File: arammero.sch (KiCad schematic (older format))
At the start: 21 parts

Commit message: Improvements
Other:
- note added: "TODO pillanatérték?"
- note removed: "Kell másik műveleti erősítő: pl \nMC33204DR2G\nrail-to-rail, +-3.3V-ról fog járni, nagy közös módusú elnyomás"

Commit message: correct  op amp type to rail-to-rail
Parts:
- U6: renamed from U?; value TL084 -> mc33204
- gave numbers to parts that had none: 16

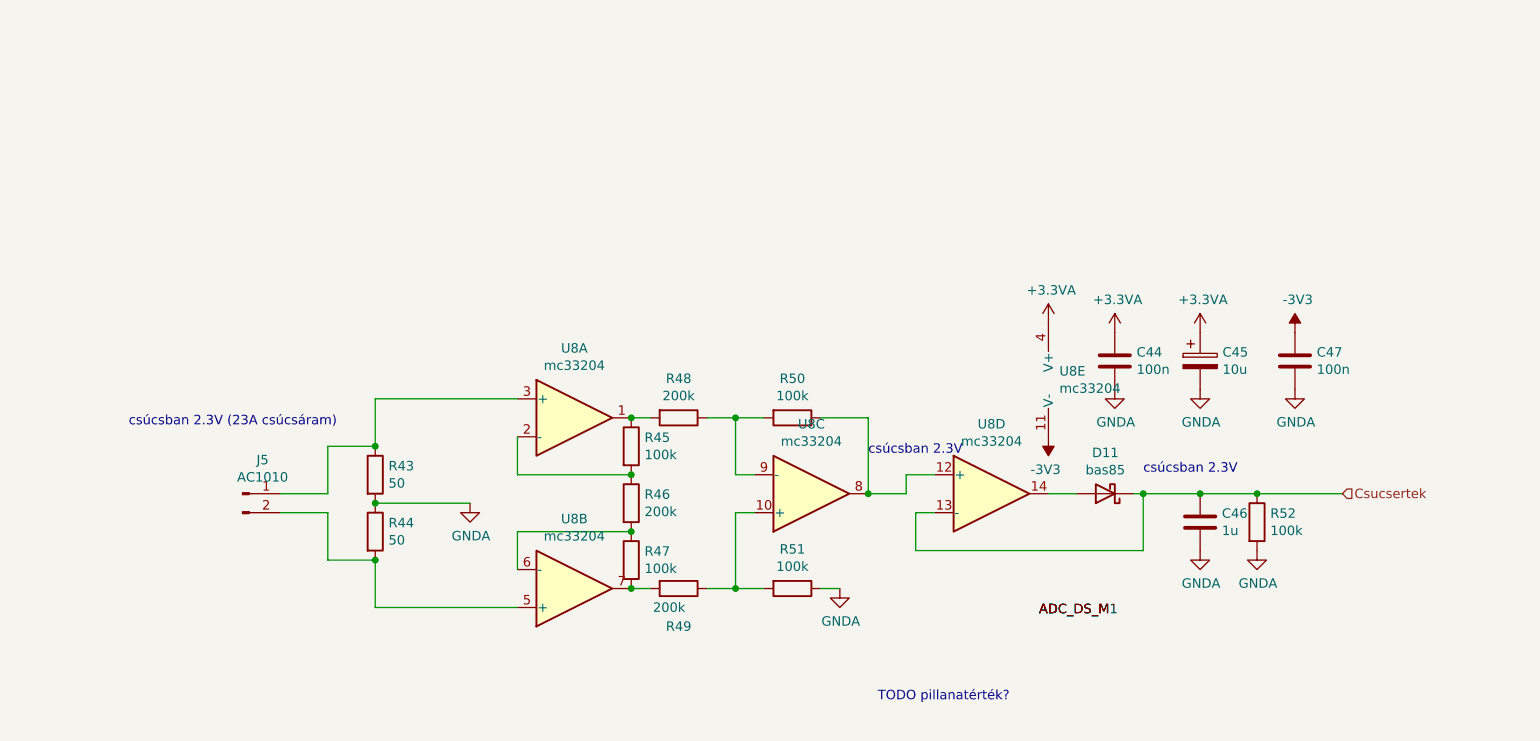
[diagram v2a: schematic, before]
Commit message: Tápegység külön lap + fázisméréshez áramkörök
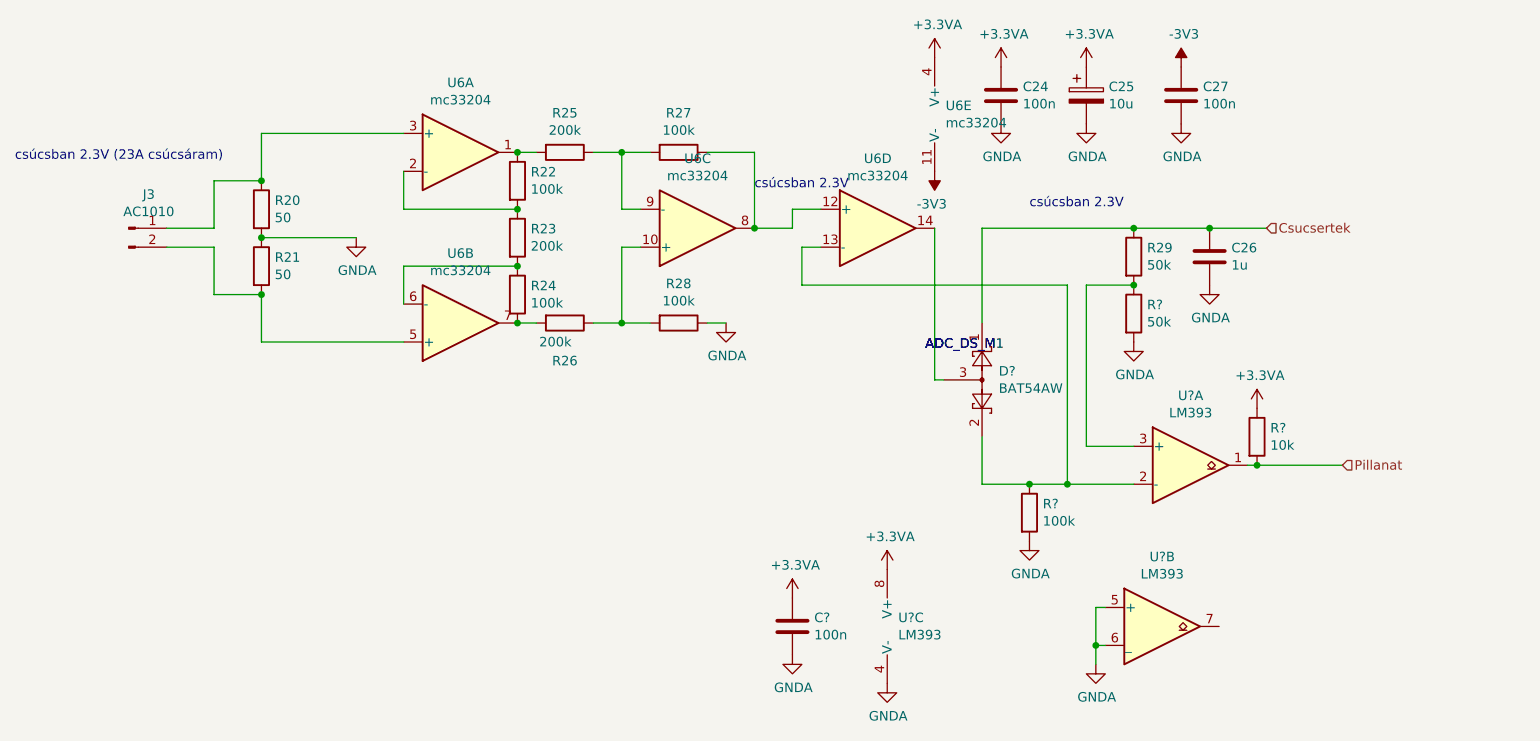
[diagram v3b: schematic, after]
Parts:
- removed D10: bas85, symbol Device:D_Schottky
- added C?: 100n, symbol Device:C
- added D?: BAT54AW, Package_TO_SOT_SMD:SOT-323_SC-70, symbol Diode:BAT54AW
- added R?: 50k, symbol Device:R
- added R?: 100k, symbol Device:R
- added R?: 10k, symbol Device:R
- added U? (x3): LM393, symbol Comparator:LM393
- R29: value 100k -> 50k
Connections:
- net +3.3VA: now also C?.1, R?.1, U?.8 (V+)
- net Csucsertek: now also D?.1; no longer U6.13 (-)
- net GNDA: now also C?.2, R?.2, R?.2, U?.4 (V-), U?.5 (+), U?.6 (_); no longer R29.2
- net at U6.14: now also D?.3
- new net: D?.2, R?.1, U6.13 (-), U?.2 (-)
- new net: R29.2, R?.1, U?.3 (+)
- new net Pillanat: R?.2, U?.1
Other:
- note removed: "TODO pillanatérték?"
- moved on the sheet: C24, C25, C26, C27, J3, R20, R21, R22, R23, R24, R25, R26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

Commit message: Testpoints + ground connections
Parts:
- added TP? (x4): TestPoint, symbol Connector:TestPoint
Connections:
- net Csucsertek: now also TP?.1
- net Pillanat: now also TP?.1
- net at R27.1, U6.12 (+), U6.8: now also TP?.1
- net at D?.2, R?.1, U6.13 (-)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: now also TP?.1
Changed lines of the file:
@@
 Csucsertek
 Wire Wire Line
-	5650 2600 5850 2600
+	5650 2600 5800 2600
 Text HLabel 8750 3850 2    50   Input ~ 0
 Pillanat
@@
 $EndComp
 Wire Wire Line
-	7650 2600 8050 2600
+	7650 2600 7900 2600
 Connection ~ 8050 2600
 Wire Wire Line
@@
 Connection ~ 8300 3850
 Wire Wire Line
-	8300 3850 8750 3850
+	8300 3850 8600 3850
 Wire Wire Line
 	7300 2900 7300 3950
@@
 	6850 3700 6850 3950
 Wire Wire Line
-	6850 3950 7100 3950
+	6850 3950 6900 3950
 Wire Wire Line
 	6850 3100 6850 2600
@@
 Wire Wire Line
 	6600 2600 6600 3400
+$Comp
+L Connector:TestPoint TP?
+U 1 1 5F898268
+P 5800 2650
+F 0 "TP?" H 5743 2676 50  0000 R CNN
+F 1 "TestPoint" H 5743 2767 50  0000 R CNN
+F 2 "" H 6000 2650 50  0001 C CNN
+F 3 "~" H 6000 2650 50  0001 C CNN
+	1    5800 2650
+	1    0    0    1
+$EndComp
+Wire Wire Line
+	5800 2650 5800 2600
+Connection ~ 5800 2600
+Wire Wire Line
+	5800 2600 5850 2600
+$Comp
+L Connector:TestPoint TP?
+U 1 1 5F89C1AC
+P 7900 2550
+F 0 "TP?" H 7842 2668 50  0000 R CNN
+F 1 "TestPoint" H 7842 2577 50  0000 R CNN
+F 2 "" H 8100 2550 50  0001 C CNN
+F 3 "~" H 8100 2550 50  0001 C CNN
+	1    7900 2550
+	-1   0    0    -1
+$EndComp
+Wire Wire Line
+	7900 2550 7900 2600
+Connection ~ 7900 2600
+Wire Wire Line
+	7900 2600 8050 2600
+$Comp
+L Connector:TestPoint TP?
+U 1 1 5F8A1D27
+P 8600 3800
+F 0 "TP?" H 8542 3918 50  0000 R CNN
+F 1 "TestPoint" H 8542 3827 50  0000 R CNN
+F 2 "" H 8800 3800 50  0001 C CNN
+F 3 "~" H 8800 3800 50  0001 C CNN
+	1    8600 3800
+	-1   0    0    -1
+$EndComp
+Wire Wire Line
+	8600 3800 8600 3850
+Connection ~ 8600 3850
+Wire Wire Line
+	8600 3850 8750 3850
+$Comp
+L Connector:TestPoint TP?
+U 1 1 5F8A4E56
+P 6900 3850
+F 0 "TP?" H 6842 3968 50  0000 R CNN
+F 1 "TestPoint" H 6842 3877 50  0000 R CNN
+F 2 "" H 7100 3850 50  0001 C CNN
+F 3 "~" H 7100 3850 50  0001 C CNN
+	1    6900 3850
+	-1   0    0    -1
+$EndComp
+Wire Wire Line
+	6900 3850 6900 3950
+Connection ~ 6900 3950
+Wire Wire Line
+	6900 3950 7100 3950
 $EndSCHEMATC

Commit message: ++
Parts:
- removed C25: 10u, symbol mosogep-rescue:CP-Device
- added C13, C36: 4u7, Capacitor_SMD:C_1206_3216Metric_Pad1.33x1.80mm_HandSolder, symbol Device:C
- added R28, R29: 1M, Resistor_SMD:R_0805_2012Metric_Pad1.20x1.40mm_HandSolder, symbol Device:R
- C11: renamed from C?; footprint (none) -> Capacitor_SMD:C_0805_2012Metric_Pad1.18x1.45mm_HandSolder
- C12: renamed from C24; footprint (none) -> Capacitor_SMD:C_0805_2012Metric_Pad1.18x1.45mm_HandSolder
- C14: renamed from C27; footprint (none) -> Capacitor_SMD:C_0805_2012Metric_Pad1.18x1.45mm_HandSolder
- C15: renamed from C26; footprint (none) -> Capacitor_SMD:C_0805_2012Metric_Pad1.18x1.45mm_HandSolder
- J2: renamed from J3; footprint (none) -> Connector_Molex:Molex_SL_171971-0002_1x02_P2.54mm_Vertical
- R16: renamed from R20; footprint (none) -> Resistor_SMD:R_0805_2012Metric_Pad1.20x1.40mm_HandSolder
- R17: renamed from R21; footprint (none) -> Resistor_SMD:R_0805_2012Metric_Pad1.20x1.40mm_HandSolder
- R18: renamed from R22; footprint (none) -> Resistor_SMD:R_0805_2012Metric_Pad1.20x1.40mm_HandSolder
- R19: renamed from R23; footprint (none) -> Resistor_SMD:R_0805_2012Metric_Pad1.20x1.40mm_HandSolder
- R20: renamed from R24; footprint (none) -> Resistor_SMD:R_0805_2012Metric_Pad1.20x1.40mm_HandSolder
- R21: renamed from R25; footprint (none) -> Resistor_SMD:R_0805_2012Metric_Pad1.20x1.40mm_HandSolder
- R22: renamed from R26; footprint (none) -> Resistor_SMD:R_0805_2012Metric_Pad1.20x1.40mm_HandSolder
- R23: renamed from R27; footprint (none) -> Resistor_SMD:R_0805_2012Metric_Pad1.20x1.40mm_HandSolder
- R24: renamed from R28; footprint (none) -> Resistor_SMD:R_0805_2012Metric_Pad1.20x1.40mm_HandSolder
- R25, R27, R30: renamed from R?; footprint (none) -> Resistor_SMD:R_0805_2012Metric_Pad1.20x1.40mm_HandSolder
- R26: renamed from R29; footprint (none) -> Resistor_SMD:R_0805_2012Metric_Pad1.20x1.40mm_HandSolder
- TP1, TP2, TP3, TP4: renamed from TP?; footprint (none) -> Connector_Pin:Pin_D0.9mm_L10.0mm_W2.4mm_FlatFork
- U3: renamed from U6; footprint (none) -> Package_SO:SOIC-14_3.9x8.7mm_P1.27mm
- U4: renamed from U?; footprint (none) -> Package_SO:SOIC-8_3.9x4.9mm_P1.27mm
- gave numbers to parts that had none: 1
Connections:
- net +3.3VA: now also C13.1, C36.1
- net GNDA: now also U4.7, C13.2, C36.2
- net Pillanat: now also R29.1
- net at J2.1 (Pin_1), R16.1: now also U3.5 (+); no longer U3.3 (+)
- net at J2.2 (Pin_2), R17.2: now also U3.3 (+); no longer U3.5 (+)
- net at R18.1, R21.2: now also U3.7; no longer U3.1
- net at R18.2, R19.1: now also U3.6 (-); no longer U3.2 (-)
- net at R19.2, R20.1: now also U3.2 (-); no longer U3.6 (-)
- net at R20.2, R22.2: now also U3.1; no longer U3.7
- net at D10.2, R25.1, TP2.1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: now also U4.3 (+), R28.1; no longer U4.2 (-)
- net at R26.2, R27.1: now also U4.2 (-); no longer U4.3 (+)
- new net: R28.2, R29.2
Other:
- moved on the sheet: C42, R74, TP12, U8A, U8B

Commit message: Bottom silk
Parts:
- added D22: LED, LED_SMD:LED_0805_2012Metric_Pad1.15x1.40mm_HandSolder, symbol Device:LED
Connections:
- net Pillanat renamed Fazismeres
- net Fazismeres: now also D22.1 (K); no longer R30.2
- new net: D22.2 (A), R30.2
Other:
- moved on the sheet: R89
